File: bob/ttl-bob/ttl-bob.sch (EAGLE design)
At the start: 33 parts, among them U1 SN65LVDS1, U2 SN65LVDS2, U3 SN65LVDS1, U4 SN65LVDS2, U5 SN65LVDS1, U6 SN65LVDS1

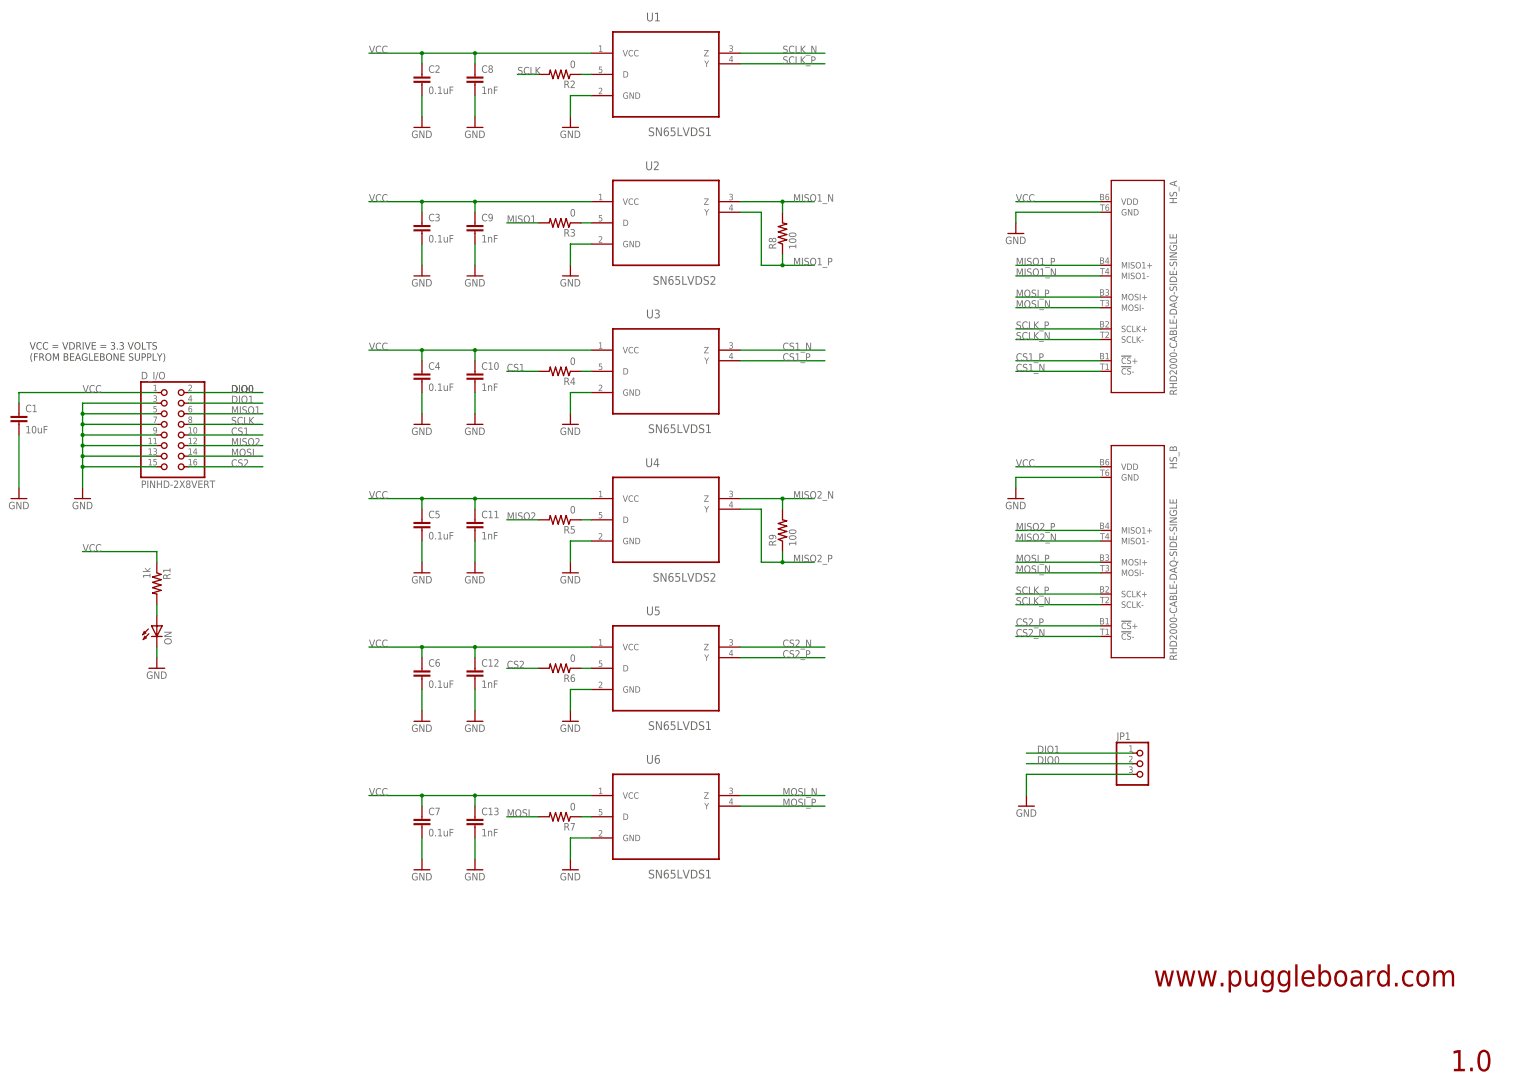
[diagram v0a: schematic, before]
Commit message: Added a CMOS to TTL BOB.
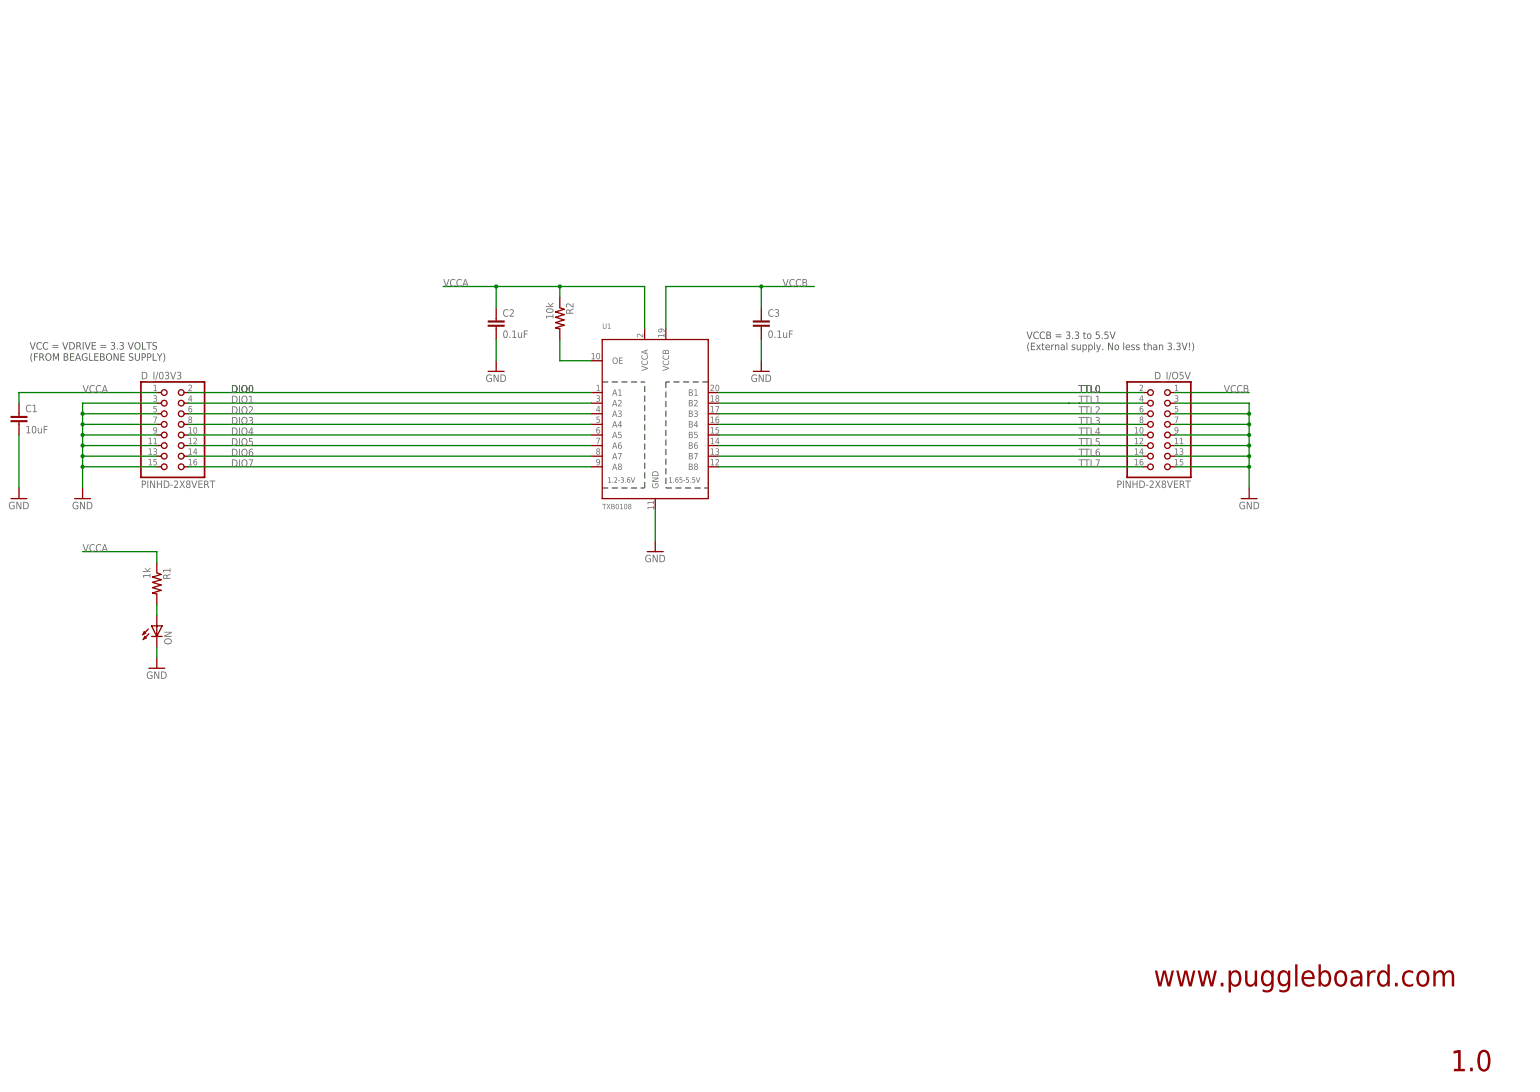
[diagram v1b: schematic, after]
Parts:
- removed C10, C11, C12, C13, C8, C9: 1nF, puggleboard:C_0603
- removed C4, C5, C6, C7: 0.1uF, puggleboard:C_0603
- removed HS_A, HS_B: RHD2000-CABLE-DAQ-SIDE-SINGLE, puggleboard:RHD2000-CABLE-DAQ-SIDE-SINGLE
- removed JP1: (no value), adafruit:PINHD-1X3
- removed R3, R4, R5, R6, R7: 0, puggleboard:R_0603
- removed R8, R9: 100, puggleboard:R_0603
- removed U2, U4: SN65LVDS2, ti-extended:SN65LVDS2DBVR
- removed U3, U5, U6: SN65LVDS1, ti-extended:SN65LVDS1DBVR
- added D_I/O5V: PINHD-2X8VERT, adafruit:PINHD-2X8VERT
- R2: value 0 -> 10k
- U1: value SN65LVDS1 -> TXB0108; device ti-extended:SN65LVDS1DBVR -> adafruit:TXB0108PWR; DIGIKEY 296-6919-1-ND -> (none)
- renumbered D_I/O to D_I/03V3
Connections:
- removed net CS1: D_I/03V3.10, R4.2
- removed net CS1_N: HS_A.!CS!-, U3.Z
- removed net CS1_P: HS_A.!CS!+, U3.Y
- removed net CS2: D_I/03V3.16, R6.2
- removed net CS2_N: HS_B.!CS!-, U5.Z
- removed net CS2_P: HS_B.!CS!+, U5.Y
- removed net MISO1: D_I/03V3.6, R3.2
- removed net MISO1_N: HS_A.MISO1-, R8.2, U2.Z
- removed net MISO1_P: HS_A.MISO1+, R8.1, U2.Y
- removed net MISO2: D_I/03V3.12, R5.2
- removed net MISO2_N: HS_B.MISO1-, R9.2, U4.Z
- removed net MISO2_P: HS_B.MISO1+, R9.1, U4.Y
- removed net MOSI: D_I/03V3.14, R7.2
- removed net MOSI_N: HS_A.MOSI-, HS_B.MOSI-, U6.Z
- removed net MOSI_P: HS_A.MOSI+, HS_B.MOSI+, U6.Y
- removed net N$2: R3.1, U2.D
- removed net N$3: R4.1, U3.D
- removed net N$4: R5.1, U4.D
- removed net N$5: R6.1, U5.D
- removed net N$6: R7.1, U6.D
- removed net SCLK: D_I/03V3.8, R2.2
- removed net SCLK_N: HS_A.SCLK-, HS_B.SCLK-, U1.Z
- removed net SCLK_P: HS_A.SCLK+, HS_B.SCLK+, U1.Y
- removed net VCC: C1.1, C10.1, C11.1, C12.1, C13.1, C2.1, C3.1, C4.1, C5.1, C6.1, C7.1, C8.1, C9.1, D_I/03V3.1, HS_A.VDD, HS_B.VDD, R1.1, U1.VCC, U2.VCC, U3.VCC, U4.VCC, U5.VCC, U6.VCC
- new net DIO2: D_I/03V3.6, U1.A3
- new net DIO3: D_I/03V3.8, U1.A4
- new net DIO4: D_I/03V3.10, U1.A5
- new net DIO5: D_I/03V3.12, U1.A6
- new net DIO6: D_I/03V3.14, U1.A7
- new net DIO7: D_I/03V3.16, U1.A8
- new net TTL0: D_I/O5V.2, U1.B1
- new net TTL1: D_I/O5V.4, U1.B2
- new net TTL2: D_I/O5V.6, U1.B3
- new net TTL3: D_I/O5V.8, U1.B4
- new net TTL4: D_I/O5V.10, U1.B5
- new net TTL5: D_I/O5V.12, U1.B6
- new net TTL6: D_I/O5V.14, U1.B7
- new net TTL7: D_I/O5V.16, U1.B8
- new net VCCA: C1.1, C2.1, D_I/03V3.1, R1.1, R2.1, U1.VCCA
- new net VCCB: C3.1, D_I/O5V.1, U1.VCCB
- net DIO0: now also U1.A1; no longer JP1.2
- net DIO1: now also U1.A2; no longer JP1.1
- net GND: now also D_I/O5V.11, D_I/O5V.13, D_I/O5V.15, D_I/O5V.3, D_I/O5V.5, D_I/O5V.7, D_I/O5V.9; no longer C10.2, C11.2, C12.2, C13.2, C4.2, C5.2, C6.2, C7.2, C8.2, C9.2, HS_A.GND, HS_B.GND, JP1.3, U2.GND, U3.GND, U4.GND, U5.GND, U6.GND
- net N$7: now also R2.2, U1.OE; no longer R2.1, U1.D
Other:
- note added: "VCCB = 3.3 to 5.5V (External supply. No less than 3.3V!)"
- moved on the sheet: C2, C3, R2

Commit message: Starting consolodating PuggleBoard library and adding part attributes containing DK part numbers.
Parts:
- removed D_I/O5V: PINHD-2X8VERT, adafruit:PINHD-2X8VERT
- added D_I/O5V0: PINHD-2X8FEMALEVERT, puggleboard:PINHD-2X8FEMALEVERT
- D_I/03V3: value PINHD-2X8VERT -> PINHD-2X8FEMALEVERT; device adafruit:PINHD-2X8VERT -> puggleboard:PINHD-2X8FEMALEVERT
- ON: value LED-CHIP0805 -> LEDGREEN-CHIP0805; device puggleboard:LED-CHIP0805 -> puggleboard:LEDGREEN-CHIP0805
- U1: device adafruit:TXB0108PWR -> puggleboard:TXB0108PWR
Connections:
- net GND: now also D_I/O5V0.11, D_I/O5V0.13, D_I/O5V0.15, D_I/O5V0.3, D_I/O5V0.5, D_I/O5V0.7, D_I/O5V0.9; no longer D_I/O5V.11, D_I/O5V.13, D_I/O5V.15, D_I/O5V.3, D_I/O5V.5, D_I/O5V.7, D_I/O5V.9
- net TTL0: now also D_I/O5V0.2; no longer D_I/O5V.2
- net TTL1: now also D_I/O5V0.4; no longer D_I/O5V.4
- net TTL2: now also D_I/O5V0.6; no longer D_I/O5V.6
- net TTL3: now also D_I/O5V0.8; no longer D_I/O5V.8
- net TTL4: now also D_I/O5V0.10; no longer D_I/O5V.10
- net TTL5: now also D_I/O5V0.12; no longer D_I/O5V.12
- net TTL6: now also D_I/O5V0.14; no longer D_I/O5V.14
- net TTL7: now also D_I/O5V0.16; no longer D_I/O5V.16
- net VCCB: now also D_I/O5V0.1; no longer D_I/O5V.1
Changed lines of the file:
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@@
 </classes>
 <parts>
-<part name="D_I/03V3" library="adafruit" deviceset="PINHD-2X8" device="VERT" value="PINHD-2X8VERT"/>
+<part name="D_I/03V3" library="puggleboard" deviceset="PINHD-2X8" device="VERT" technology="FEMALE" value="PINHD-2X8FEMALEVERT"/>
 <part name="GND16" library="supply1" deviceset="GND" device=""/>
 <part name="C1" library="puggleboard" deviceset="C" device="_0805" value="10uF"/>
 <part name="GND22" library="supply1" deviceset="GND" device=""/>
-<part name="ON" library="puggleboard" deviceset="LED" device="-CHIP0805" value=""/>
+<part name="ON" library="puggleboard" deviceset="LED" device="-CHIP0805" technology="GREEN" value="LEDGREEN-CHIP0805"/>
 <part name="R1" library="puggleboard" deviceset="R" device="_0603" value="1k"/>
 <part name="GND24" library="supply1" deviceset="GND" device=""/>
 <part name="FRAME1" library="frames" deviceset="FRAME_B_L" device=""/>
-<part name="D_I/O5V" library="adafruit" deviceset="PINHD-2X8" device="VERT" value="PINHD-2X8VERT"/>
+<part name="D_I/O5V0" library="puggleboard" deviceset="PINHD-2X8" device="VERT" technology="FEMALE" value="PINHD-2X8FEMALEVERT"/>
 <part name="GND20" library="supply1" deviceset="GND" device=""/>
-<part name="U1" library="adafruit" deviceset="TXB0108PWR" device="" value="TXB0108"/>
+<part name="U1" library="puggleboard" deviceset="TXB0108PWR" device="" value="TXB0108"/>
 <part name="GND1" library="supply1" deviceset="GND" device=""/>
 <part name="C2" library="puggleboard" deviceset="C" device="_0603" value="0.1uF"/>
@@
 <instance part="FRAME1" gate="G$1" x="-223.52" y="-175.26"/>
 <instance part="FRAME1" gate="G$2" x="101.6" y="-175.26"/>
-<instance part="D_I/O5V" gate="G$1" x="121.92" y="-17.78" rot="MR0"/>
+<instance part="D_I/O5V0" gate="G$1" x="121.92" y="-17.78" rot="MR0"/>
 <instance part="GND20" gate="1" x="142.24" y="-33.02" rot="MR0"/>
 <instance part="U1" gate="G$1" x="0" y="-12.7"/>
@@
 <wire x1="142.24" y1="-10.16" x2="142.24" y2="-12.7" width="0.1524" layer="91"/>
 <junction x="142.24" y="-12.7"/>
-<pinref part="D_I/O5V" gate="G$1" pin="15"/>
-<pinref part="D_I/O5V" gate="G$1" pin="13"/>
-<pinref part="D_I/O5V" gate="G$1" pin="11"/>
-<pinref part="D_I/O5V" gate="G$1" pin="3"/>
-<pinref part="D_I/O5V" gate="G$1" pin="5"/>
-<pinref part="D_I/O5V" gate="G$1" pin="7"/>
-<pinref part="D_I/O5V" gate="G$1" pin="9"/>
+<pinref part="D_I/O5V0" gate="G$1" pin="15"/>
+<pinref part="D_I/O5V0" gate="G$1" pin="13"/>
+<pinref part="D_I/O5V0" gate="G$1" pin="11"/>
+<pinref part="D_I/O5V0" gate="G$1" pin="3"/>
+<pinref part="D_I/O5V0" gate="G$1" pin="5"/>
+<pinref part="D_I/O5V0" gate="G$1" pin="7"/>
+<pinref part="D_I/O5V0" gate="G$1" pin="9"/>
 <pinref part="GND20" gate="1" pin="GND"/>
 </segment>
@@
 <net name="TTL0" class="0">
 <segment>
-<pinref part="D_I/O5V" gate="G$1" pin="2"/>
+<pinref part="D_I/O5V0" gate="G$1" pin="2"/>
 <label x="106.68" y="-7.62" size="1.778" layer="95" rot="MR0"/>
 <label x="106.68" y="-7.62" size="1.778" layer="95" rot="MR0"/>
@@
 <net name="TTL1" class="0">
 <segment>
-<pinref part="D_I/O5V" gate="G$1" pin="4"/>
+<pinref part="D_I/O5V0" gate="G$1" pin="4"/>
 <wire x1="116.84" y1="-10.16" x2="101.6" y2="-10.16" width="0.1524" layer="91"/>
 <label x="106.68" y="-10.16" size="1.778" layer="95" rot="MR0"/>
@@
 <net name="TTL2" class="0">
 <segment>
-<pinref part="D_I/O5V" gate="G$1" pin="6"/>
+<pinref part="D_I/O5V0" gate="G$1" pin="6"/>
 <label x="106.68" y="-12.7" size="1.778" layer="95" rot="MR0"/>
 <pinref part="U1" gate="G$1" pin="B3"/>
@@
 <net name="TTL3" class="0">
 <segment>
-<pinref part="D_I/O5V" gate="G$1" pin="8"/>
+<pinref part="D_I/O5V0" gate="G$1" pin="8"/>
 <label x="106.68" y="-15.24" size="1.778" layer="95" rot="MR0"/>
 <pinref part="U1" gate="G$1" pin="B4"/>
@@
 <net name="TTL4" class="0">
 <segment>
-<pinref part="D_I/O5V" gate="G$1" pin="10"/>
+<pinref part="D_I/O5V0" gate="G$1" pin="10"/>
 <label x="106.68" y="-17.78" size="1.778" layer="95" rot="MR0"/>
 <pinref part="U1" gate="G$1" pin="B5"/>
@@
 <net name="TTL5" class="0">
 <segment>
-<pinref part="D_I/O5V" gate="G$1" pin="12"/>
+<pinref part="D_I/O5V0" gate="G$1" pin="12"/>
 <label x="106.68" y="-20.32" size="1.778" layer="95" rot="MR0"/>
 <pinref part="U1" gate="G$1" pin="B6"/>
@@
 <net name="TTL6" class="0">
 <segment>
-<pinref part="D_I/O5V" gate="G$1" pin="14"/>
+<pinref part="D_I/O5V0" gate="G$1" pin="14"/>
 <label x="106.68" y="-22.86" size="1.778" layer="95" rot="MR0"/>
 <pinref part="U1" gate="G$1" pin="B7"/>
@@
 <net name="TTL7" class="0">
 <segment>
-<pinref part="D_I/O5V" gate="G$1" pin="16"/>
+<pinref part="D_I/O5V0" gate="G$1" pin="16"/>
 <label x="106.68" y="-25.4" size="1.778" layer="95" rot="MR0"/>
 <pinref part="U1" gate="G$1" pin="B8"/>
@@
 <segment>
 <wire x1="124.46" y1="-7.62" x2="142.24" y2="-7.62" width="0.1524" layer="91"/>
-<pinref part="D_I/O5V" gate="G$1" pin="1"/>
+<pinref part="D_I/O5V0" gate="G$1" pin="1"/>
 <label x="142.24" y="-7.62" size="1.778" layer="95" rot="MR0"/>
 </segment>

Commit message: Started looking into BOM-EX ULP for part database managment. Not sure if this is the right choice.
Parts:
- R1: DK (none) -> P1.00KHCT-ND; MPN (none) -> ERJ-3EKF1001V
- R2: DK (none) -> P10.0KHCT-ND; MPN (none) -> ERJ-3EKF1002V
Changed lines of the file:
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@@
 <schematic xreflabel="%F%N/%S.%C%R" xrefpart="/%S.%C%R">
 <attributes>
+<attribute name="DATABASE" value="./bom/PARTS-DB.TXT"/>
 </attributes>
 <variantdefs>
@@
 <part name="GND22" library="supply1" deviceset="GND" device=""/>
 <part name="ON" library="puggleboard" deviceset="LED" device="-CHIP0805" technology="GREEN" value="LEDGREEN-CHIP0805"/>
-<part name="R1" library="puggleboard" deviceset="R" device="_0603" value="1k"/>
+<part name="R1" library="puggleboard" deviceset="R" device="_0603" value="1k">
+<attribute name="DK" value="P1.00KHCT-ND"/>
+<attribute name="MPN" value="ERJ-3EKF1001V"/>
+</part>
 <part name="GND24" library="supply1" deviceset="GND" device=""/>
 <part name="FRAME1" library="frames" deviceset="FRAME_B_L" device=""/>
@@
 <part name="GND2" library="supply1" deviceset="GND" device=""/>
 <part name="GND3" library="supply1" deviceset="GND" device=""/>
-<part name="R2" library="puggleboard" deviceset="R" device="_0603" value="10k"/>
+<part name="R2" library="puggleboard" deviceset="R" device="_0603" value="10k">
+<attribute name="DK" value="P10.0KHCT-ND"/>
+<attribute name="MPN" value="ERJ-3EKF1002V"/>
+</part>
 </parts>
 <sheets>
